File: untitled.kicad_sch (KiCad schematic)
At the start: 2 parts, among them J3 AVR-ISP-6, U1 ATmega328P-P

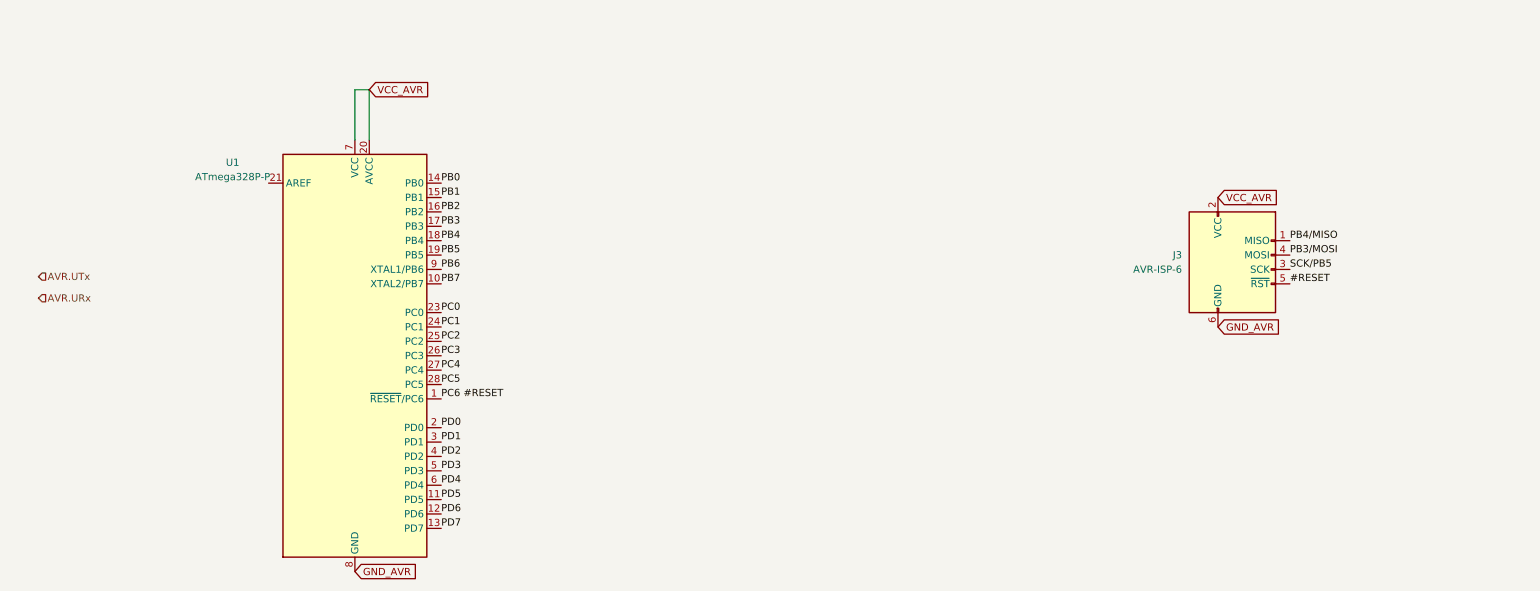
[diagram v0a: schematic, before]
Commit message: sch: finished with main components
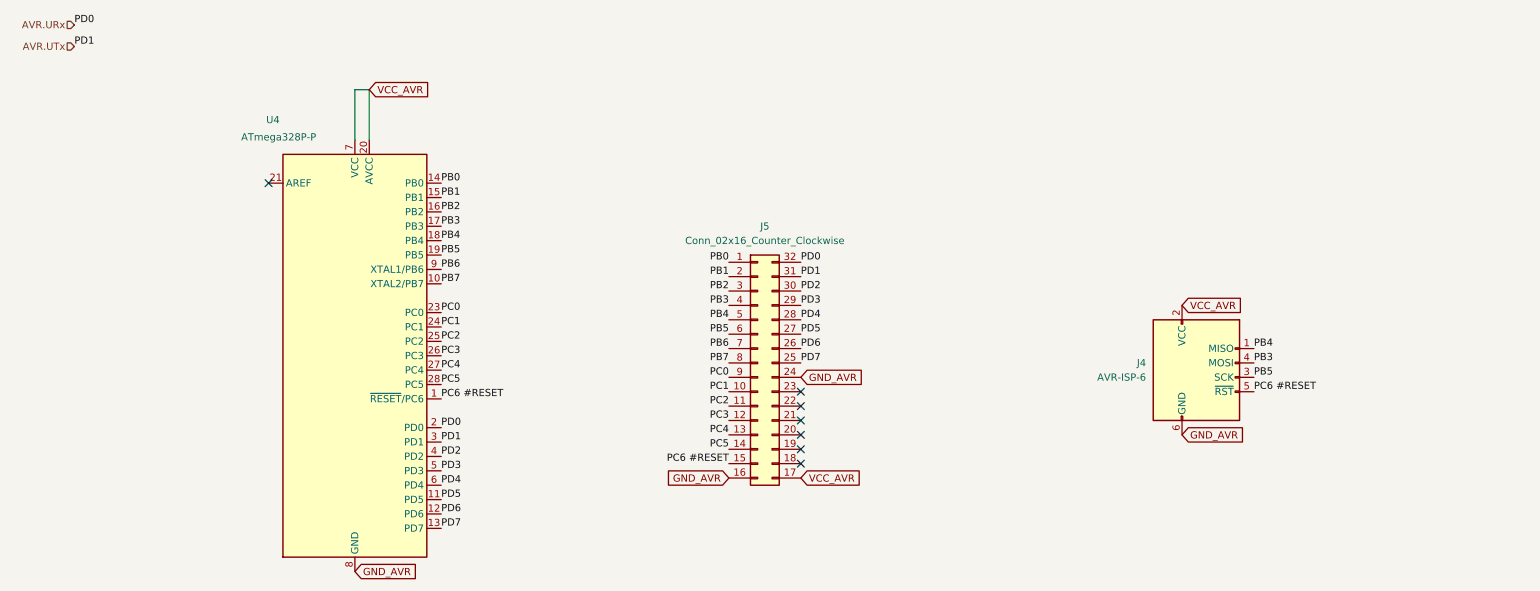
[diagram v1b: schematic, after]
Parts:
- added J5: Conn_02x16_Counter_Clockwise, symbol Connector_Generic:Conn_02x16_Counter_Clockwise
- renumbered J3 to J4, U1 to U4
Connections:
- net #RESET is gone; now on net PC6 #RESET: J4.5 (~{RST})
- net PB3/MOSI is gone; now on net PB3: J4.4 (MOSI)
- net PB4/MISO is gone; now on net PB4: J4.1 (MISO)
- net PD0 is gone; now on net AVR.URx: U4.2 (PD0)
- net PD1 is gone; now on net AVR.UTx: U4.3 (PD1)
- net SCK/PB5 is gone; now on net PB5: J4.3 (SCK)
- net AVR.URx: now also J5.32 (Pin_32)
- net AVR.UTx: now also J5.31 (Pin_31)
- net GND_AVR: now also J5.16 (Pin_16), J5.24 (Pin_24)
- net PB0: now also J5.1 (Pin_1)
- net PB1: now also J5.2 (Pin_2)
- net PB2: now also J5.3 (Pin_3)
- net PB3: now also J5.4 (Pin_4)
- net PB4: now also J5.5 (Pin_5)
- net PB5: now also J5.6 (Pin_6)
- net PB6: now also J5.7 (Pin_7)
- net PB7: now also J5.8 (Pin_8)
- net PC0: now also J5.9 (Pin_9)
- net PC1: now also J5.10 (Pin_10)
- net PC2: now also J5.11 (Pin_11)
- net PC3: now also J5.12 (Pin_12)
- net PC4: now also J5.13 (Pin_13)
- net PC5: now also J5.14 (Pin_14)
- net PC6 #RESET: now also J5.15 (Pin_15)
- net PD2: now also J5.30 (Pin_30)
- net PD3: now also J5.29 (Pin_29)
- net PD4: now also J5.28 (Pin_28)
- net PD5: now also J5.27 (Pin_27)
- net PD6: now also J5.26 (Pin_26)
- net PD7: now also J5.25 (Pin_25)
- net VCC_AVR: now also J5.17 (Pin_17)
- no-connect marks 0 -> 7
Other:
- company: (none) -> HugonLabs
- title: (none) -> AVR328-USB
- moved on the sheet: J4

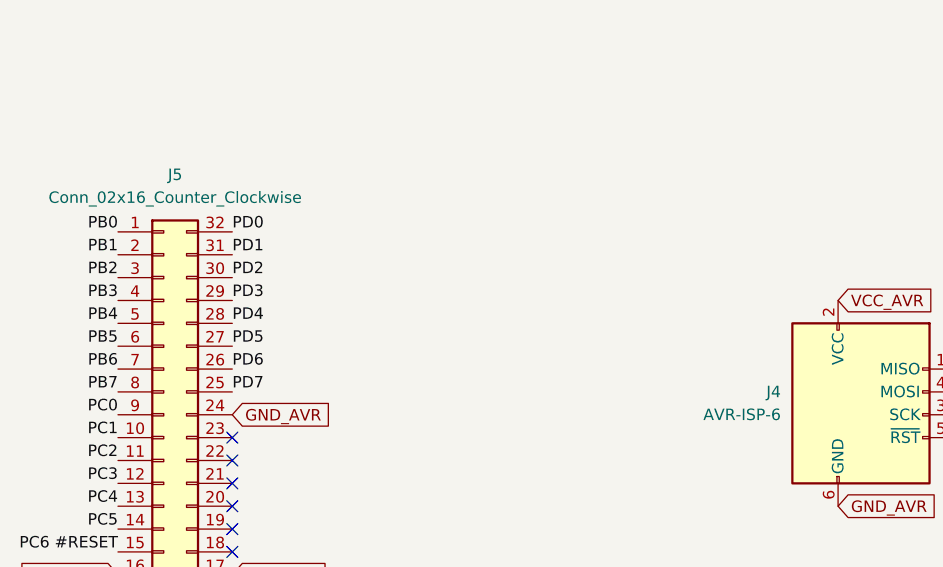
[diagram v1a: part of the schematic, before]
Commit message: sch: done, footprints added as well
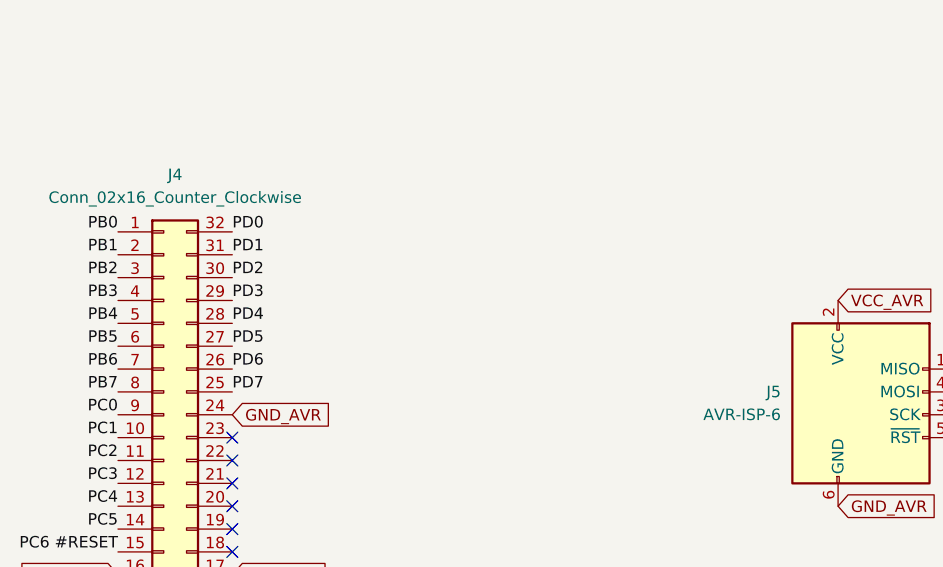
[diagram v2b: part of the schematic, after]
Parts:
- J4: renamed from J5; footprint (none) -> Connector_PinHeader_2.54mm:PinHeader_2x16_P2.54mm_Vertical
- J5: renamed from J4; footprint (none) -> Connector_PinHeader_2.54mm:PinHeader_2x03_P2.54mm_Vertical
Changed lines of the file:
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@@
 		(dnp no)
 		(fields_autoplaced yes)
-		(property "Reference" "J4"
+		(property "Reference" "J5"
 			(at 214.63 78.7399 0)
 			(effects
@@
 			)
 		)
-		(property "Footprint" ""
+		(property "Footprint" "Connector_PinHeader_2.54mm:PinHeader_2x03_P2.54mm_Vertical"
 			(at 217.17 80.01 90)
 			(effects
@@
 			(project "avr328usbc"
 				(path "/e7a067a8-1d75-4b62-a93c-d6508c6150f1/6ead66d4-fbd0-44c7-9236-cc34a95896d0"
-					(reference "J4")
+					(reference "J5")
 					(unit 1)
 				)
@@
 		(dnp no)
 		(fields_autoplaced yes)
-		(property "Reference" "J5"
+		(property "Reference" "J4"
 			(at 147.32 54.61 0)
 			(effects
@@
 			)
 		)
-		(property "Footprint" ""
+		(property "Footprint" "Connector_PinHeader_2.54mm:PinHeader_2x16_P2.54mm_Vertical"
 			(at 146.05 78.74 0)
 			(effects
@@
 			(project "avr328usbc"
 				(path "/e7a067a8-1d75-4b62-a93c-d6508c6150f1/6ead66d4-fbd0-44c7-9236-cc34a95896d0"
-					(reference "J5")
+					(reference "J4")
 					(unit 1)
 				)

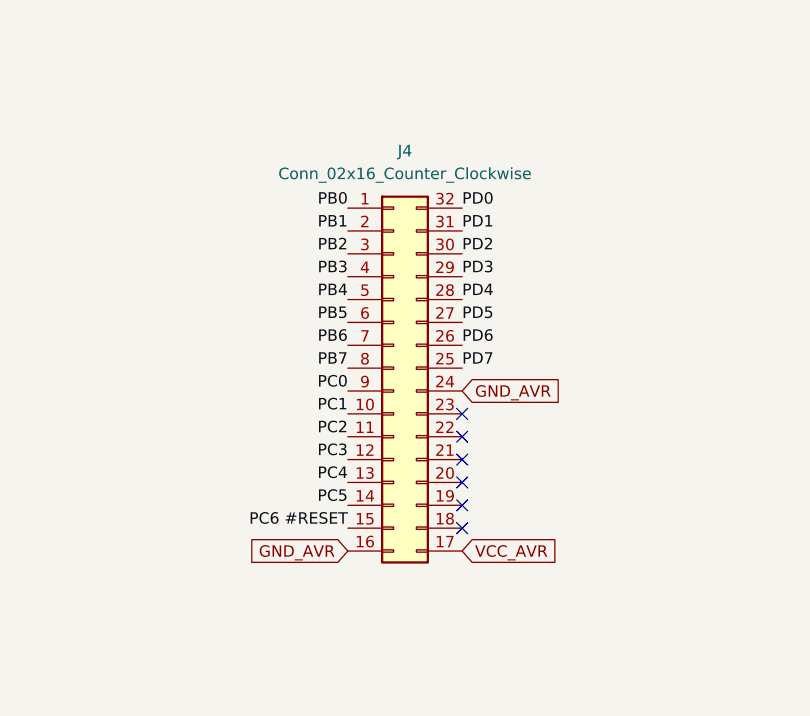
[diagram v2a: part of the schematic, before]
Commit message: finished converting schematic to correct USBC and pin headers
Symbols didn't match the footprints
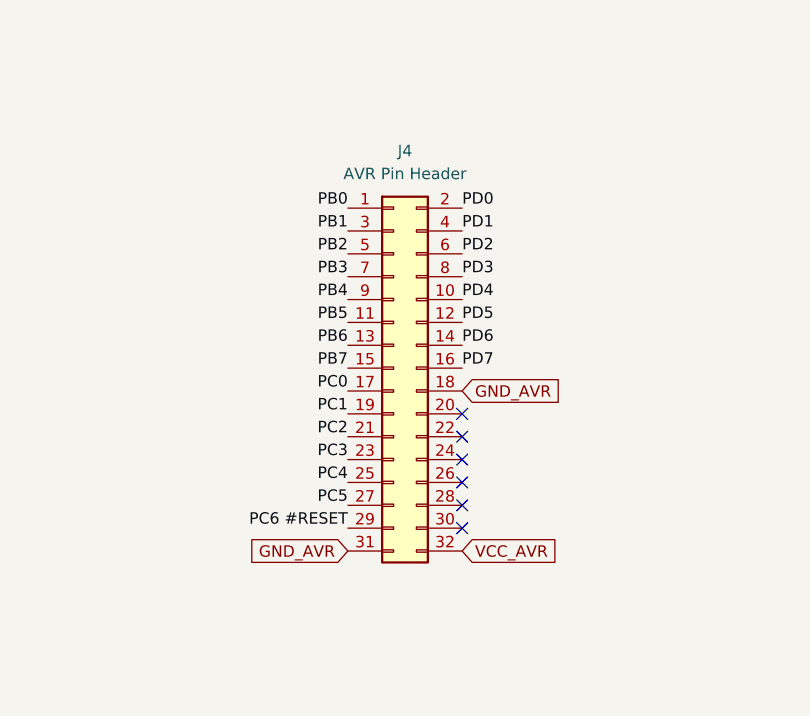
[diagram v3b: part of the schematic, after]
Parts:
- J4: value Conn_02x16_Counter_Clockwise -> AVR Pin Header; symbol Connector_Generic:Conn_02x16_Counter_Clockwise -> Connector_Generic:Conn_02x16_Odd_Even; MFR (none) -> Amphenol
- J5: MFR (none) -> Amphenol
- U4: MFR (none) -> Microchip; MFR Part Num (none) -> ATmega328P-PU
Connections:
- net AVR.URx: now also J4.2 (Pin_2); no longer J4.32 (Pin_32)
- net AVR.UTx: now also J4.4 (Pin_4); no longer J4.31 (Pin_31)
- net GND_AVR: now also J4.18 (Pin_18), J4.31 (Pin_31); no longer J4.16 (Pin_16), J4.24 (Pin_24)
- net PB1: now also J4.3 (Pin_3); no longer J4.2 (Pin_2)
- net PB2: now also J4.5 (Pin_5); no longer J4.3 (Pin_3)
- net PB3: now also J4.7 (Pin_7); no longer J4.4 (Pin_4)
- net PB4: now also J4.9 (Pin_9); no longer J4.5 (Pin_5)
- net PB5: now also J4.11 (Pin_11); no longer J4.6 (Pin_6)
- net PB6: now also J4.13 (Pin_13); no longer J4.7 (Pin_7)
- net PB7: now also J4.15 (Pin_15); no longer J4.8 (Pin_8)
- net PC0: now also J4.17 (Pin_17); no longer J4.9 (Pin_9)
- net PC1: now also J4.19 (Pin_19); no longer J4.10 (Pin_10)
- net PC2: now also J4.21 (Pin_21); no longer J4.11 (Pin_11)
- net PC3: now also J4.23 (Pin_23); no longer J4.12 (Pin_12)
- net PC4: now also J4.25 (Pin_25); no longer J4.13 (Pin_13)
- net PC5: now also J4.27 (Pin_27); no longer J4.14 (Pin_14)
- net PC6 #RESET: now also J4.29 (Pin_29); no longer J4.15 (Pin_15)
- net PD2: now also J4.6 (Pin_6); no longer J4.30 (Pin_30)
- net PD3: now also J4.8 (Pin_8); no longer J4.29 (Pin_29)
- net PD4: now also J4.10 (Pin_10); no longer J4.28 (Pin_28)
- net PD5: now also J4.12 (Pin_12); no longer J4.27 (Pin_27)
- net PD6: now also J4.14 (Pin_14); no longer J4.26 (Pin_26)
- net PD7: now also J4.16 (Pin_16); no longer J4.25 (Pin_25)
- net VCC_AVR: now also J4.32 (Pin_32); no longer J4.17 (Pin_17)
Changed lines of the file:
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@@
+			)
+		)
+		(property "MFR" "Amphenol"
+			(at 223.52 81.28 0)
+			(effects
+				(font
+					(size 1.27 1.27)
+				)
+				(hide yes)
+			)
+		)
+		(property "MFR Part Num" ""
+			(at 223.52 81.28 0)
+			(effects
+				(font
+					(size 1.27 1.27)
+				)
+				(hide yes)
 			)
 		)
@@
 	)
 	(symbol
-		(lib_id "Connector_Generic:Conn_02x16_Counter_Clockwise")
+		(lib_id "Connector_Generic:Conn_02x16_Odd_Even")
 		(at 146.05 78.74 0)
 		(unit 1)
@@
 			)
 		)
-		(property "Value" "Conn_02x16_Counter_Clockwise"
+		(property "Value" "AVR Pin Header"
 			(at 147.32 57.15 0)
 			(effects
@@
 			)
 		)
-		(property "Description" "Generic connector, double row, 02x16, counter clockwise pin numbering scheme (similar to DIP package numbering), script generated (kicad-library-utils/schlib/autogen/connector/)"
+		(property "Description" "Generic connector, double row, 02x16, odd/even pin numbering scheme (row 1 odd numbers, row 2 even numbers), script generated (kicad-library-utils/schlib/autogen/connector/)"
+			(at 146.05 78.74 0)
+			(effects
+				(font
+					(size 1.27 1.27)
+				)
+				(hide yes)
+			)
+		)
+		(property "MFR" "Amphenol"
+			(at 146.05 78.74 0)
+			(effects
+				(font
+					(size 1.27 1.27)
+				)
+				(hide yes)
+			)
+		)
+		(property "MFR Part Num" ""
 			(at 146.05 78.74 0)
 			(effects
@@
 			(at 74.93 77.47 0)
 			(effects
+				(font
+					(size 1.27 1.27)
+				)
+				(hide yes)
+			)
+		)
+		(property "MFR" "Microchip"
+			(at 74.93 77.47 0)
+			(effects
+				(font
+					(size 1.27 1.27)
+				)
+				(hide yes)
+			)
+		)
+		(property "MFR Part Num" "ATmega328P-PU"
+			(at 74.93 77.47 0)
+			(effects

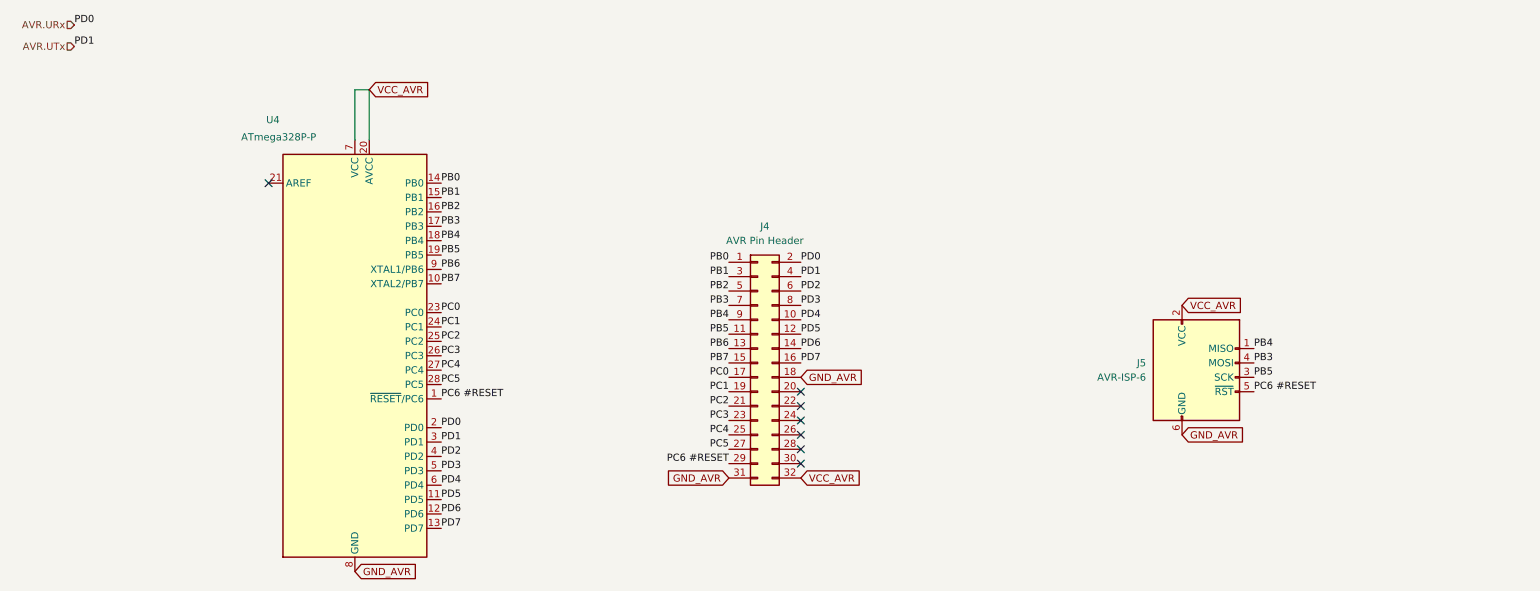
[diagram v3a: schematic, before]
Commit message: changed AVR header into 2 headers mirroring pinout
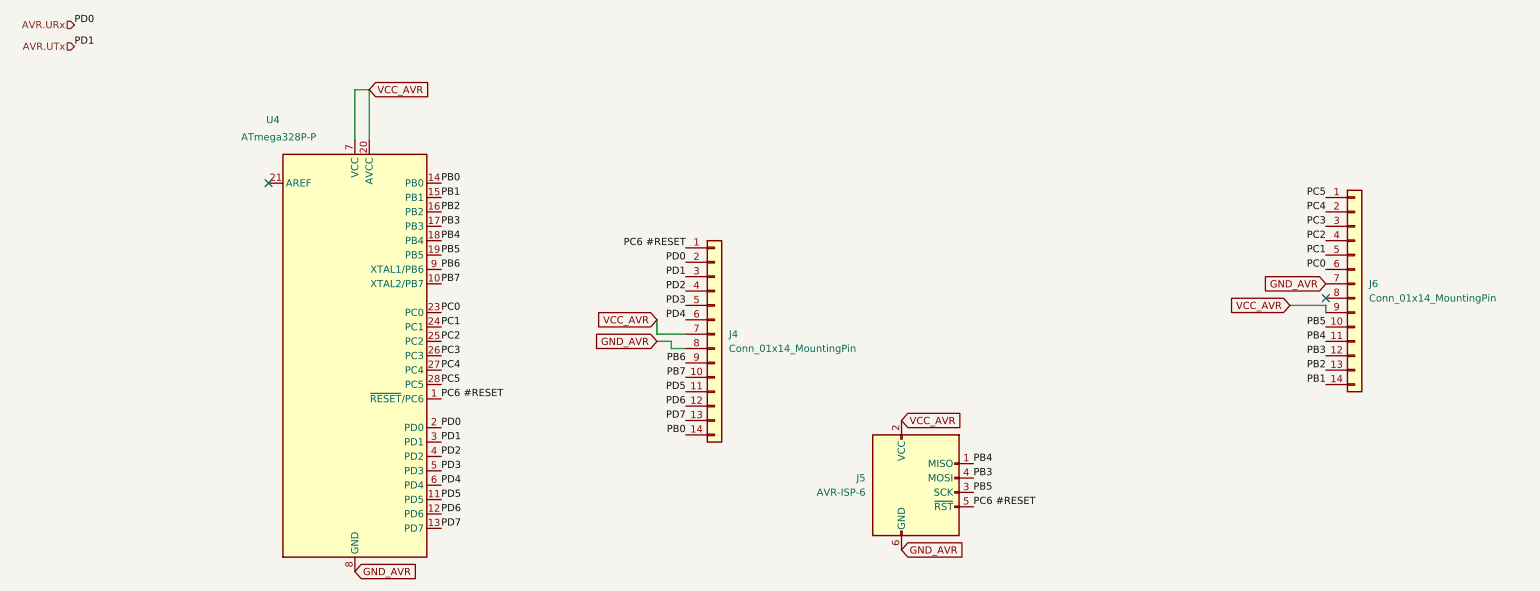
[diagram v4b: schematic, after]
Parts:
- removed J4: AVR Pin Header, Connector_PinHeader_2.54mm:PinHeader_2x16_P2.54mm_Vertical, symbol Connector_Generic:Conn_02x16_Odd_Even
- added J4, J6: Conn_01x14_MountingPin, symbol Connector_Generic:Conn_01x14
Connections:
- net AVR.URx: now also J4.2 (Pin_2)
- net AVR.UTx: now also J4.3 (Pin_3)
- net GND_AVR: now also J4.8 (Pin_8), J6.7 (Pin_7)
- net PB0: now also J4.14 (Pin_14)
- net PB1: now also J6.14 (Pin_14)
- net PB2: now also J6.13 (Pin_13)
- net PB3: now also J6.12 (Pin_12)
- net PB4: now also J6.11 (Pin_11)
- net PB5: now also J6.10 (Pin_10)
- net PB6: now also J4.9 (Pin_9)
- net PB7: now also J4.10 (Pin_10)
- net PC0: now also J6.6 (Pin_6)
- net PC1: now also J6.5 (Pin_5)
- net PC2: now also J6.4 (Pin_4)
- net PC3: now also J6.3 (Pin_3)
- net PC4: now also J6.2 (Pin_2)
- net PC5: now also J6.1 (Pin_1)
- net PC6 #RESET: now also J4.1 (Pin_1)
- net PD2: now also J4.4 (Pin_4)
- net PD3: now also J4.5 (Pin_5)
- net PD4: now also J4.6 (Pin_6)
- net PD5: now also J4.11 (Pin_11)
- net PD6: now also J4.12 (Pin_12)
- net PD7: now also J4.13 (Pin_13)
- net VCC_AVR: now also J4.7 (Pin_7), J6.9 (Pin_9)
- no-connect marks 7 -> 2
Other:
- moved on the sheet: J5
